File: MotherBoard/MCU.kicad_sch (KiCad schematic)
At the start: 48 parts, among them J201 Conn_ARM_SWD_TagConnect_TC2030, J202 DM3AT-SF-PEJM5_40_, U201 STM32F205RBTx, Y201 16 Mhz

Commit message: Added more 3D models
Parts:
- C201, C216: footprint (none) -> Capacitor_SMD:C_0603_1608Metric
- C202, C203, C204, C205, C206, C207, C208, C209, C210, C211, C212, C213, C214, C215, L201: footprint (none) -> Capacitor_SMD:C_0402_1005Metric
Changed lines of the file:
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@@
 			)
 		)
-		(property "Footprint" ""
+		(property "Footprint" "Capacitor_SMD:C_0603_1608Metric"
 			(at 235.9152 90.17 0)
 			(effects
@@
 			)
 		)
-		(property "Footprint" ""
+		(property "Footprint" "Capacitor_SMD:C_0402_1005Metric"
 			(at 120.3452 86.36 0)
 			(effects
@@
 			)
 		)
-		(property "Footprint" ""
+		(property "Footprint" "Capacitor_SMD:C_0402_1005Metric"
 			(at 131.7752 86.36 0)
 			(effects
@@
 			)
 		)
-		(property "Footprint" ""
+		(property "Footprint" "Capacitor_SMD:C_0402_1005Metric"
 			(at 47.9552 124.46 0)
 			(effects
@@
 			)
 		)
-		(property "Footprint" ""
+		(property "Footprint" "Capacitor_SMD:C_0402_1005Metric"
 			(at 224.4852 90.17 0)
 			(effects
@@
 			)
 		)
-		(property "Footprint" ""
+		(property "Footprint" "Capacitor_SMD:C_0402_1005Metric"
 			(at 20.0152 124.46 0)
 			(effects
@@
 			)
 		)
-		(property "Footprint" ""
+		(property "Footprint" "Capacitor_SMD:C_0402_1005Metric"
 			(at 135.5852 48.26 0)
 			(effects
@@
 			)
 		)
-		(property "Footprint" ""
+		(property "Footprint" "Capacitor_SMD:C_0402_1005Metric"
 			(at 154.6352 86.36 0)
 			(effects
@@
 			)
 		)
-		(property "Footprint" ""
+		(property "Footprint" "Capacitor_SMD:C_0603_1608Metric"
 			(at 20.0152 86.36 0)
 			(effects
@@
 			)
 		)
-		(property "Footprint" ""
+		(property "Footprint" "Capacitor_SMD:C_0402_1005Metric"
 			(at 70.8152 86.36 0)
 			(effects
@@
 			)
 		)
-		(property "Footprint" ""
+		(property "Footprint" "Capacitor_SMD:C_0402_1005Metric"
 			(at 32.7152 86.36 0)
 			(effects
@@
 			)
 		)
-		(property "Footprint" ""
+		(property "Footprint" "Capacitor_SMD:C_0402_1005Metric"
 			(at 142.24 76.2 0)
 			(effects
@@
 			)
 		)
-		(property "Footprint" ""
+		(property "Footprint" "Capacitor_SMD:C_0402_1005Metric"
 			(at 83.5152 86.36 0)
 			(effects
@@
 			)
 		)
-		(property "Footprint" ""
+		(property "Footprint" "Capacitor_SMD:C_0402_1005Metric"
 			(at 60.6552 170.18 0)
 			(effects
@@
 			)
 		)
-		(property "Footprint" ""
+		(property "Footprint" "Capacitor_SMD:C_0402_1005Metric"
 			(at 58.1152 86.36 0)
 			(effects
@@
 			)
 		)
-		(property "Footprint" ""
+		(property "Footprint" "Capacitor_SMD:C_0402_1005Metric"
 			(at 45.4152 86.36 0)
 			(effects
@@
 			)
 		)
-		(property "Footprint" ""
+		(property "Footprint" "Capacitor_SMD:C_0402_1005Metric"
 			(at 73.3552 170.18 0)
 			(effects

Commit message: Fixed relative paths + 90% footprints done + organized PCB for layout + found JLC part #s for manufacturing
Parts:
- D201, D202, D203, D204, D205, D206, D207, D208, D209, D210, D211, D212: Manufacturer_Part_Number (none) -> PESD3V3L1BA,115

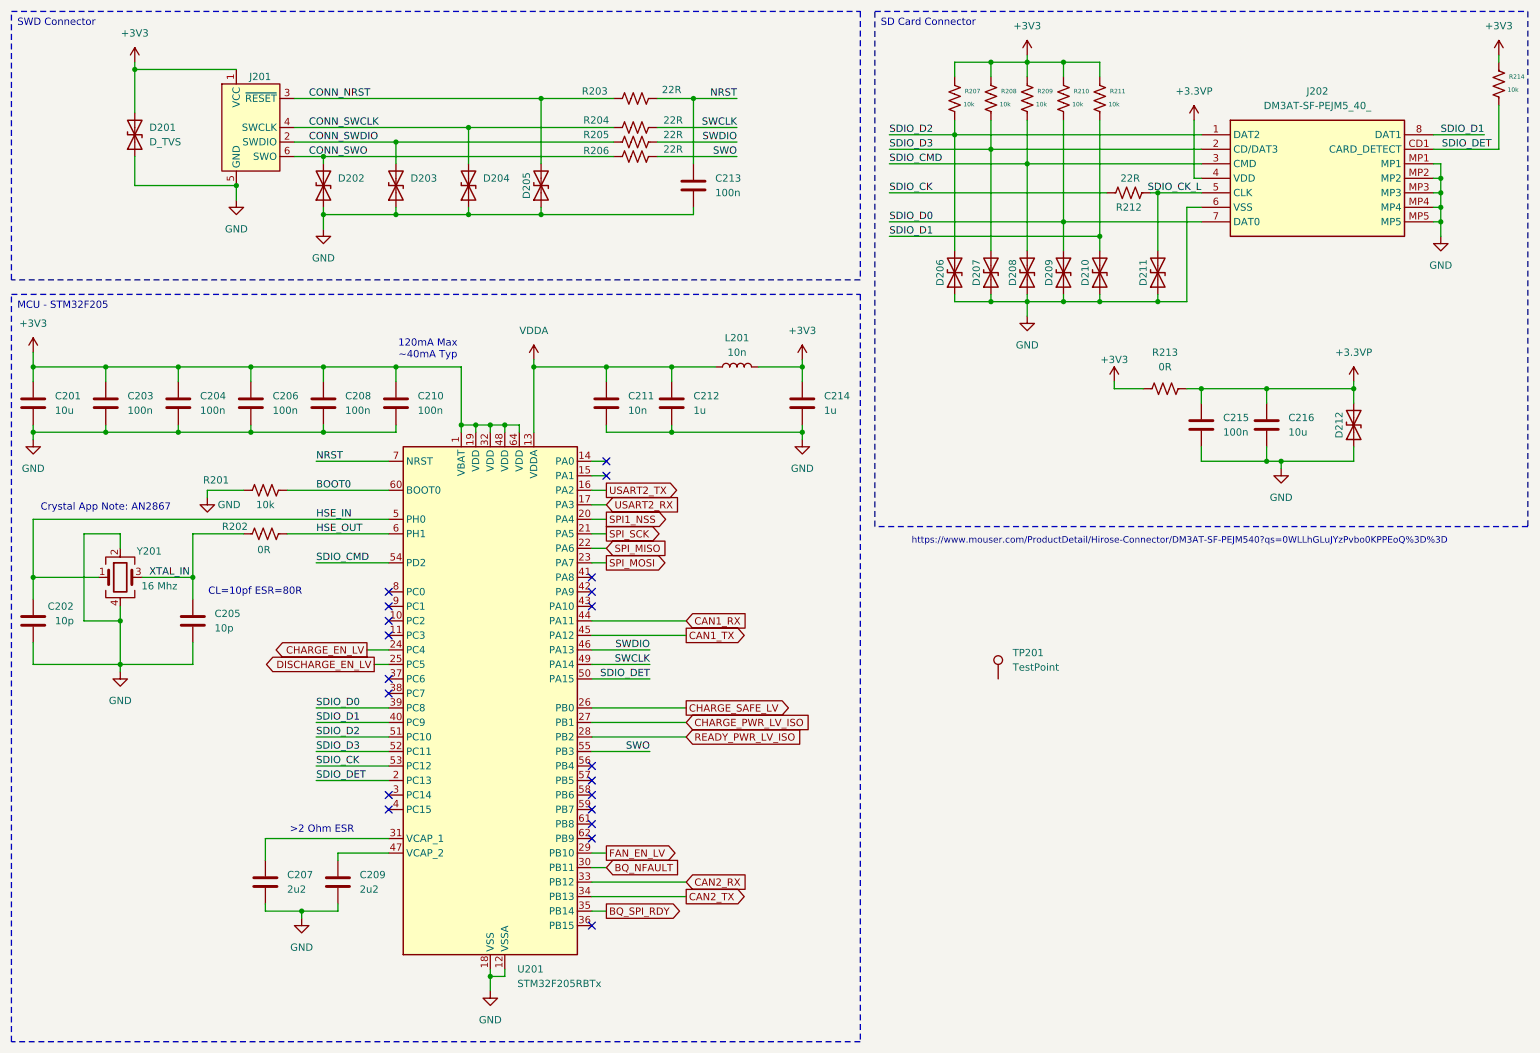
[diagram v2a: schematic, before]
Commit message: Completed BOM except inductors
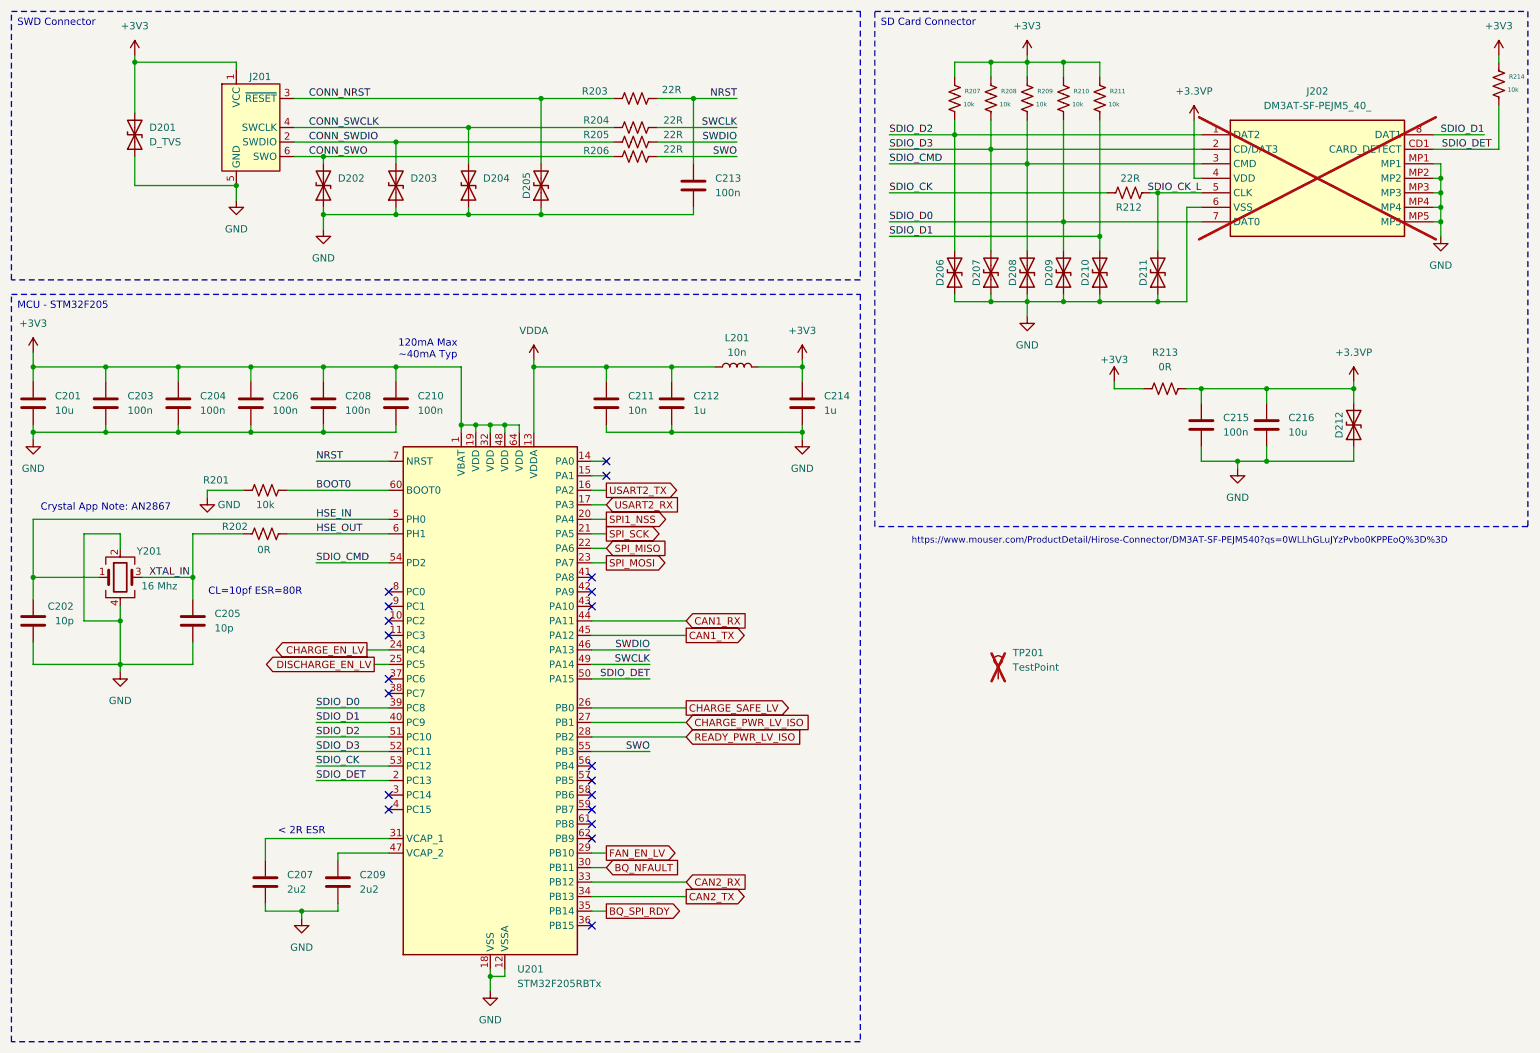
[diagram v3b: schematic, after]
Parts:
- C201, C216: Manufacturer_Part_Number (none) -> CL10A106KP8NNNC
- C202, C205: Manufacturer_Part_Number (none) -> GRM1555C1H100FA01D
- C203, C204, C206, C208, C210, C213, C215: Manufacturer_Part_Number (none) -> CL05B104KO5NNNC
- C207, C209: footprint Capacitor_SMD:C_0402_1005Metric -> Resistor_SMD:R_1206_3216Metric; Manufacturer_Part_Number (none) -> CL31B225KBHNNNE
- C211: Manufacturer_Part_Number (none) -> CC0402KRX7R9BB103
- C212, C214: Manufacturer_Part_Number (none) -> CL05A105KO5NNNC
- J202: Manufacturer_Part_Number DM3AT-SF-PEJM5(40) -> (none); now not fitted
- L201: footprint Capacitor_SMD:C_0402_1005Metric -> (none)
- R201, R207, R208, R209, R210, R211, R214: Manufacturer_Part_Number (none) -> 0402WGF1001TCE
- R202: footprint Resistor_SMD:R_0402_1005Metric -> Resistor_SMD:R_0805_2012Metric; Manufacturer_Part_Number (none) -> 0805W8F0000T5E
- R203, R204, R205, R206, R212: footprint Resistor_SMD:R_0402_1005Metric -> Resistor_SMD:R_1206_3216Metric; Manufacturer_Part_Number (none) -> FRC1206J220 TS
- R213: footprint Resistor_SMD:R_0402_1005Metric -> Resistor_SMD:R_2512_6332Metric; Manufacturer_Part_Number (none) -> 25121WJ0000T4E
- TP201: now not fitted
- U201: Manufacturer_Part_Number (none) -> STM32F205RBT6
- Y201: Manufacturer_Part_Number (none) -> X322516MLB4SI
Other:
- note added: "< 2R ESR"
- note removed: ">2 Ohm ESR"

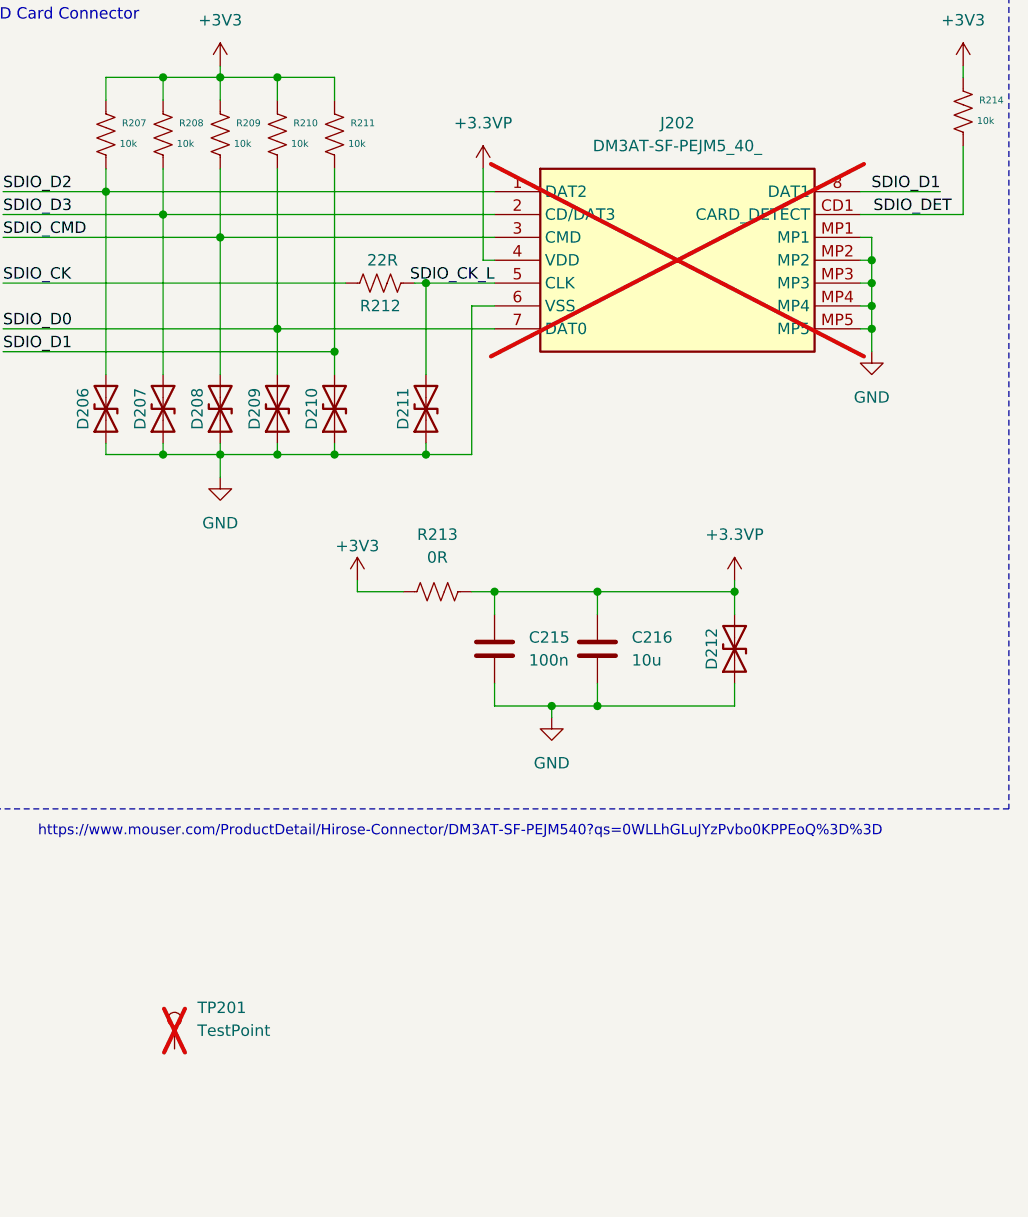
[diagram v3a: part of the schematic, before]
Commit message: BOM completed + All 3D models added + Initial board shape complete
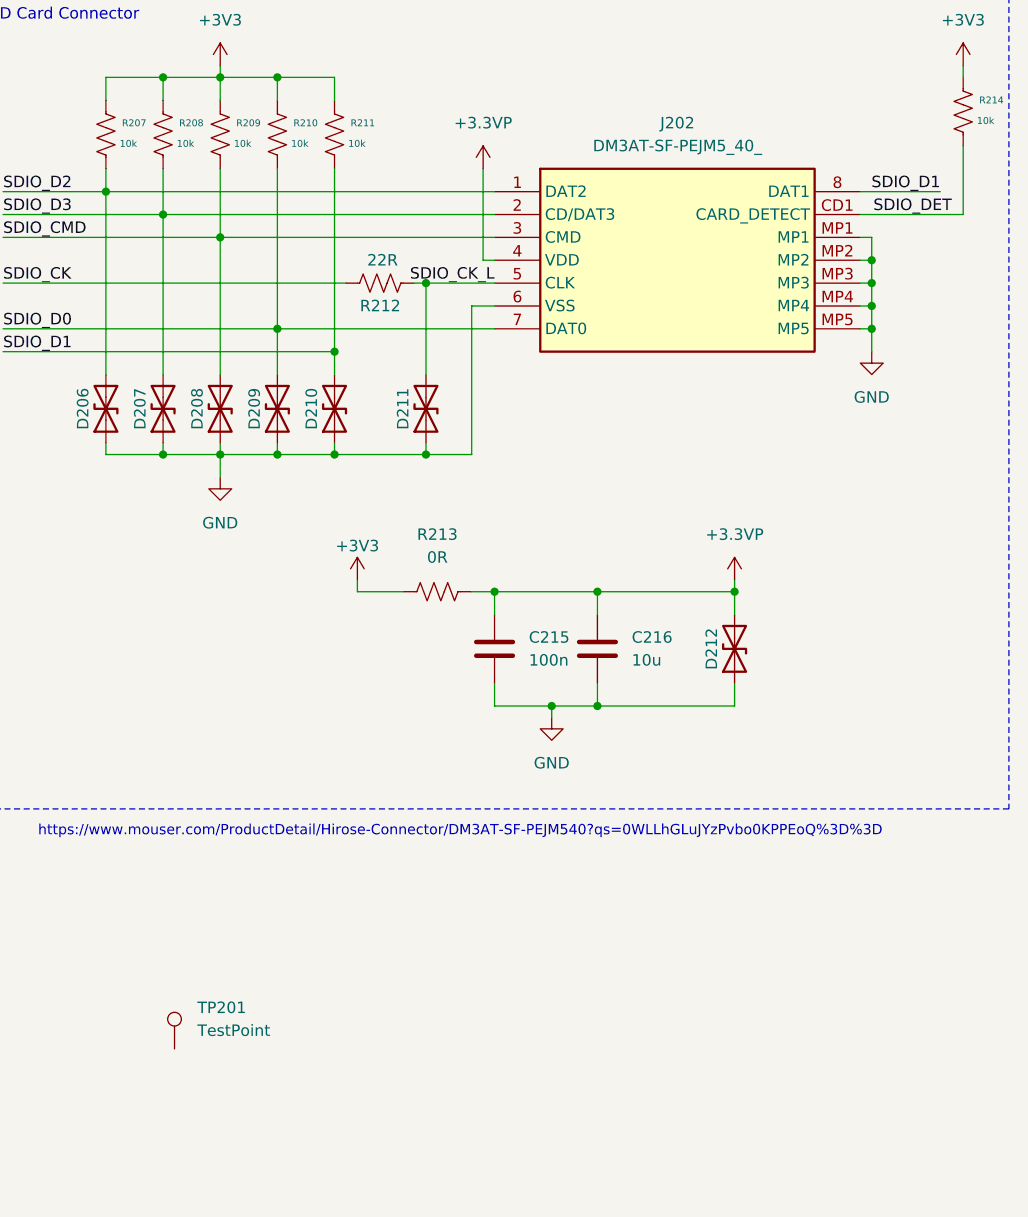
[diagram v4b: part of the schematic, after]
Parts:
- J202, TP201: now fitted
- L201: footprint (none) -> Inductor_SMD:L_0402_1005Metric; Manufacturer_Part_Number (none) -> LQG15HN10NJ02D
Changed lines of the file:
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@@
 		(in_bom yes)
 		(on_board yes)
-		(dnp yes)
+		(dnp no)
 		(fields_autoplaced yes)
 		(property "Reference" "TP201"
@@
 			)
 		)
-		(property "Footprint" ""
+		(property "Footprint" "Inductor_SMD:L_0402_1005Metric"
 			(at 142.24 76.2 0)
 			(effects
@@
 		)
 		(property "Sim.Type" ""
+			(at 142.24 76.2 0)
+			(effects
+				(font
+					(size 1.27 1.27)
+				)
+				(hide yes)
+			)
+		)
+		(property "Manufacturer_Part_Number" "LQG15HN10NJ02D"
 			(at 142.24 76.2 0)
 			(effects
@@
 		(in_bom yes)
 		(on_board yes)
-		(dnp yes)
+		(dnp no)
 		(fields_autoplaced yes)
 		(property "Reference" "J202"

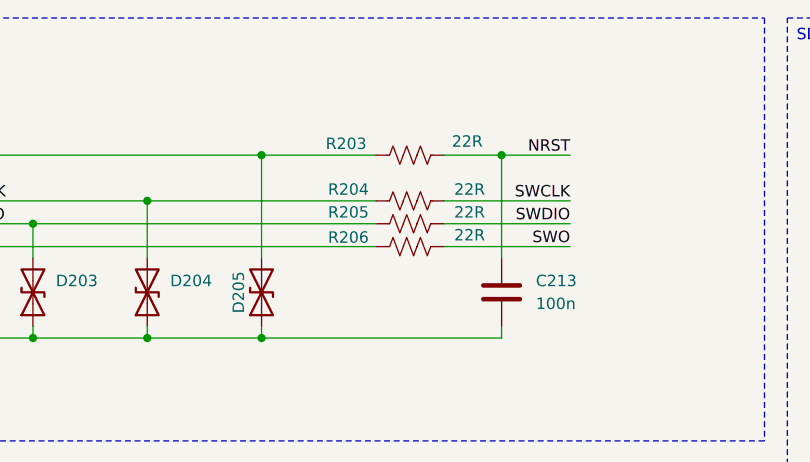
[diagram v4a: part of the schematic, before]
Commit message: Finished MCU + Tranceiver layout
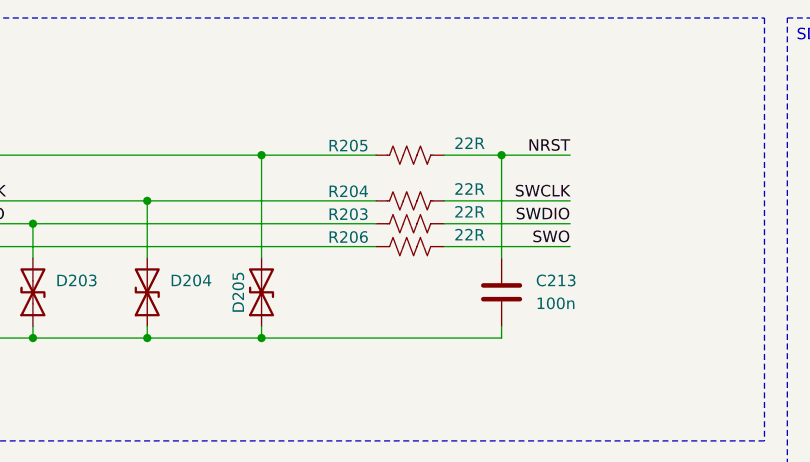
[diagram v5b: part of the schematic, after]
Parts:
- C207, C209: footprint Resistor_SMD:R_1206_3216Metric -> Capacitor_SMD:C_0603_1608Metric; Manufacturer_Part_Number CL31B225KBHNNNE -> 0603B225K250NT
- R202: footprint Resistor_SMD:R_0805_2012Metric -> Resistor_SMD:R_0402_1005Metric; Manufacturer_Part_Number 0805W8F0000T5E -> (none)
- R203, R204, R205, R206, R212: footprint Resistor_SMD:R_1206_3216Metric -> Resistor_SMD:R_0402_1005Metric; Manufacturer_Part_Number FRC1206J220 TS -> (none)
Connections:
- net CONN_NRST: now also R205.1; no longer R203.1
- net CONN_SWDIO: now also R203.1; no longer R205.1
- net NRST: now also R205.2; no longer R203.2
- net SWDIO: now also R203.2; no longer R205.2

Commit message: Finished layout need to route
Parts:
- removed D206, D207, D210: D_TVS, Diode_SMD:D_SOD-323, symbol Device:D_TVS
- removed R207, R208, R211: 10k, Resistor_SMD:R_0402_1005Metric, symbol Device:R_US
- renumbered D208 to D206, D209 to D207, D211 to D208, D212 to D209, R205 to R203, R203 to R205, R209 to R207, R210 to R208, R212 to R209, R213 to R210, R214 to R211
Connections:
- net SDIO_D1: no longer names the net of U201.40 (PC9)
- net SDIO_D1: no longer J202.8 (DAT1)
- net SDIO_D2: no longer names the net of U201.51 (PC10)
- net SDIO_D2: no longer J202.1 (DAT2)
- net SDIO_D3: no longer names the net of U201.52 (PC11)
- net SDIO_D3: no longer J202.2 (CD/DAT3)
- no-connect marks 20 -> 26
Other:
- moved on the sheet: D206, D207, D208, R207, R208, R209

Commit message: Finished motherboard. Need to review BOM
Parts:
- removed D208: D_TVS, Diode_SMD:D_SOD-323, symbol Device:D_TVS
- removed TP201: TestPoint, TestPoint:TP_5012, symbol Connector:TestPoint
- added D202: GREEN, LED_SMD:LED_0603_1608Metric, symbol Device:LED
- added R201: 1k, Resistor_SMD:R_0402_1005Metric, symbol Device:R_US
- renumbered D202 to D203, D203 to D204, D204 to D205, D205 to D206, D206 to D207, D207 to D208, R201 to R202, R202 to R203, R203 to R204, R204 to R205, R205 to R206, R206 to R207, R207 to R208, R208 to R209, R209 to R210, R210 to R211, R211 to R212
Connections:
- net GND: now also R201.2
- net SDIO_DET: no longer U201.2 (PC13)
- net TEST_LED: now reaches U201.10 (PC2)
- net TEST_LED: now also D202.2 (A)
- net UART4_TX: now reaches U201.14 (PA0)
- net UART4_RX: now reaches U201.15 (PA1)
- net ADC_IN: now reaches U201.9 (PC1)
- new net: D202.1 (K), R201.1
- no-connect marks 26 -> 23

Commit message: Fixed power routing mistake + finished BOM + generated manufacturing files
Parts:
- R203: Manufacturer_Part_Number (none) -> 0402WGF0000TCE
- R204, R205, R206, R207, R210: Manufacturer_Part_Number (none) -> 0402WGF220JTCE
